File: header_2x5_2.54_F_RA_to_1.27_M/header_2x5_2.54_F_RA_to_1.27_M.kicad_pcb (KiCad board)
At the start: 2 copper layers, 18.5 x 14 mm, 2 parts, among them J1 2.54_F_RA, J2 1.27_M

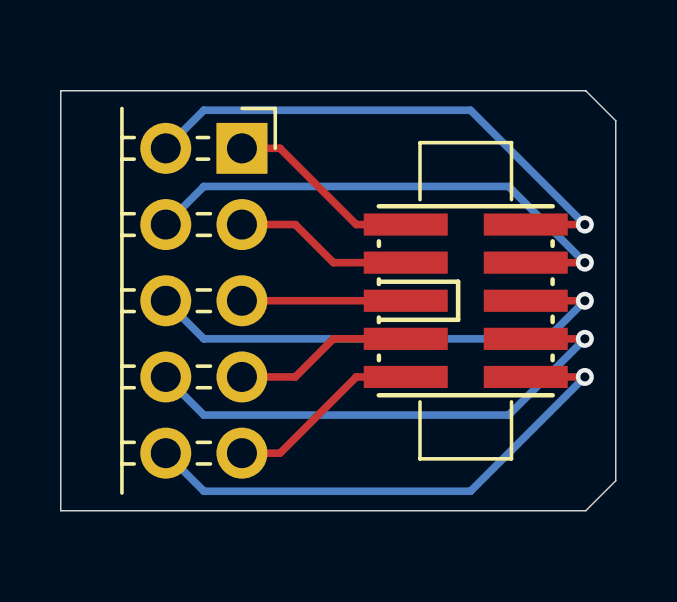
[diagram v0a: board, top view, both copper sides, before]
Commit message: Add 'header_2x5_2.54_F_RA_to_1.27_M' adapter board
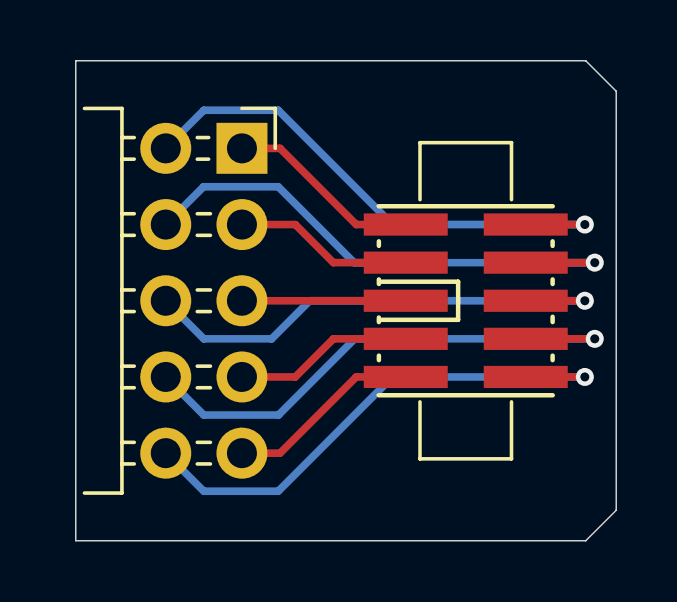
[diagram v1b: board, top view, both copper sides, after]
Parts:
- J2: footprint ng_conn:Samtec_FTSH-105-XX-X-DV -> ng_conn:Samtec_FTSH-105-XX-X-DV-Mating
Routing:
- net PIN8: track 17.5 -> 18.2 mm
- net PIN4: track 17.5 -> 18.2 mm
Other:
- board size 18.5 x 14 mm -> 18 x 16 mm
- rule pad_to_mask_clearance: 0.051 -> 0.05
- rule solder_mask_min_width: 0.25 -> 0.2
- board text added: "JTAG SWD iCE40"
- board text removed: "JTAG SWD Lattice"
